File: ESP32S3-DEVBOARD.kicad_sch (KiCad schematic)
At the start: 61 parts, among them J1 PinHeader_1x22_P2.54mm_Vertic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, J2 PinHeader_1x22_P2.54mm_Vertic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, J3 G-Switch_GT-USB-7010ASV, J4 G-Switch_GT-USB-7010ASV, Q1 BC817-40,215, Q2 BC817-40,215, SW1 TS-1088-AR02016, SW2 TS-1088-AR02016, SW3 TS-1088-AR02016, SW4 TS-1088-AR02016, U1 AMS1117-3.3, U2 ESP32-S3-WROOM-1, U3 USBLC6-2P6, U4 CP2102N-A02-GQFN28R, U5 BMI270, U6 USBLC6-2P6

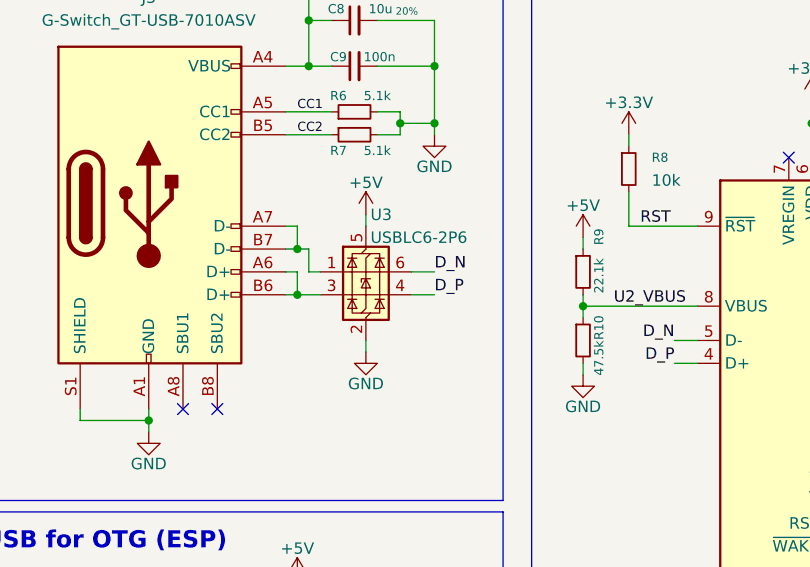
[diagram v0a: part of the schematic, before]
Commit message: Started to rout USB, need swap ports for uart
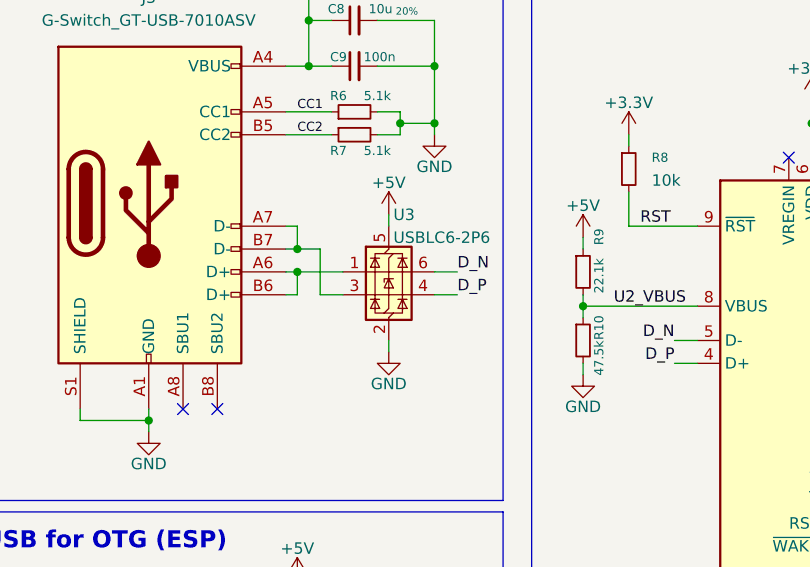
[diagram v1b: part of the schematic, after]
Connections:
- net at J3.A7 (D-), J3.B7 (D-): now also U3.3 (I/O2); no longer U3.1 (I/O1)
- net at J3.A6 (D+), J3.B6 (D+): now also U3.1 (I/O1); no longer U3.3 (I/O2)
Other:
- moved on the sheet: U3
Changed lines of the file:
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@@
 	)
 	(junction
+		(at 54.61 99.06)
+		(diameter 0)
+		(color 0 0 0 0)
+	)
+	(junction
 		(at 266.7 80.01)
 		(diameter 0)
@@
 	)
 	(junction
-		(at 54.61 101.6)
-		(diameter 0)
-		(color 0 0 0 0)
-	)
-	(junction
 		(at 185.42 123.19)
 		(diameter 0)
@@
 	(wire
 		(pts
-			(xy 64.77 147.32) (xy 64.77 148.59)
+			(xy 57.15 96.52) (xy 57.15 101.6)
 		)
 		(stroke
@@
 	(wire
 		(pts
-			(xy 208.28 39.37) (xy 209.55 39.37)
+			(xy 64.77 147.32) (xy 64.77 148.59)
 		)
 		(stroke
@@
 	(wire
 		(pts
-			(xy 54.61 101.6) (xy 57.15 101.6)
+			(xy 208.28 39.37) (xy 209.55 39.37)
 		)
 		(stroke
@@
 	(wire
 		(pts
-			(xy 67.31 99.06) (xy 69.85 99.06)
+			(xy 69.85 99.06) (xy 72.39 99.06)
 		)
 		(stroke
@@
 	(wire
 		(pts
-			(xy 62.23 106.68) (xy 62.23 107.95)
+			(xy 64.77 106.68) (xy 64.77 107.95)
 		)
 		(stroke
@@
 	(wire
 		(pts
-			(xy 55.88 99.06) (xy 57.15 99.06)
-		)
-		(stroke
-			(width 0)
-			(type default)
-		)
-	)
-	(wire
-		(pts
 			(xy 177.8 72.39) (xy 176.53 72.39)
 		)
@@
 	(wire
 		(pts
-			(xy 67.31 101.6) (xy 69.85 101.6)
+			(xy 69.85 101.6) (xy 72.39 101.6)
 		)
 		(stroke
@@
 	(wire
 		(pts
+			(xy 57.15 101.6) (xy 59.69 101.6)
+		)
+		(stroke
+			(width 0)
+			(type default)
+		)
+	)
+	(wire
+		(pts
 			(xy 177.8 62.23) (xy 176.53 62.23)
 		)
@@
 	(wire
 		(pts
-			(xy 62.23 92.71) (xy 62.23 93.98)
+			(xy 64.77 92.71) (xy 64.77 93.98)
 		)
 		(stroke
@@
 	(wire
 		(pts
-			(xy 55.88 96.52) (xy 55.88 99.06)
-		)
-		(stroke
-			(width 0)
-			(type default)
-		)
-	)
-	(wire
-		(pts
 			(xy 53.34 76.2) (xy 55.88 76.2)
 		)
@@
 	(wire
 		(pts
-			(xy 54.61 96.52) (xy 55.88 96.52)
+			(xy 54.61 96.52) (xy 57.15 96.52)
 		)
 		(stroke
@@
 	(wire
 		(pts
+			(xy 54.61 99.06) (xy 59.69 99.06)
+		)
+		(stroke
+			(width 0)
+			(type default)
+		)
+	)
+	(wire
+		(pts
 			(xy 54.61 163.83) (xy 55.88 163.83)
 		)
@@
 	)
 	(label "D_N"
-		(at 69.85 99.06 0)
+		(at 72.39 99.06 0)
 		(effects
 			(font
@@
 	)
 	(label "D_P"
-		(at 69.85 101.6 0)
+		(at 72.39 101.6 0)
 		(effects
 			(font
@@
 	(symbol
 		(lib_id "ESP32S3-DEVBOARD:USBLC6-2P6")
-		(at 62.23 99.06 0)
+		(at 64.77 99.06 0)
 		(unit 1)
 		(exclude_from_sim no)
@@
 		(dnp no)
 		(property "Reference" "U3"
-			(at 62.738 92.71 0)
+			(at 65.278 92.71 0)
 			(effects
 				(font
@@
 		)
 		(property "Value" "USBLC6-2P6"
-			(at 62.738 95.25 0)
+			(at 65.278 95.25 0)
 			(effects
 				(font
@@
 		)
 		(property "Footprint" "ESP32S3-DEVBOARD:SOT-666"
-			(at 63.246 105.791 0)
+			(at 65.786 105.791 0)
 			(effects
 				(font
@@
 		)
 		(property "Datasheet" "https://www.st.com/resource/en/datasheet/usblc6-2.pdf"
-			(at 63.246 107.696 0)
+			(at 65.786 107.696 0)
 			(effects
 				(font
@@
 		)
 		(property "Description" "Very low capacitance ESD protection diode, 2 data-line, SOT-666"
-			(at 62.23 99.06 0)
+			(at 64.77 99.06 0)
 			(effects
 				(font
@@
 		)
 		(property "Mfr. Part # " "USBLC6-2P6"
-			(at 62.23 99.06 0)
+			(at 64.77 99.06 0)
 			(effects
 				(font
@@
 		)
 		(property "LCSC" "C2827693"
-			(at 62.23 99.06 0)
+			(at 64.77 99.06 0)
 			(effects
 				(font
@@
 	(symbol
 		(lib_id "power:+5V")
-		(at 62.23 92.71 0)
+		(at 64.77 92.71 0)
 		(unit 1)
 		(exclude_from_sim no)
@@
 		(dnp no)
 		(property "Reference" "#PWR027"
-			(at 62.23 96.52 0)
+			(at 64.77 96.52 0)
 			(effects
 				(font
@@
 		)
 		(property "Value" "+5V"
-			(at 62.23 89.154 0)
+			(at 64.77 89.154 0)
 			(effects
 				(font
@@
 		)
 		(property "Footprint" ""
-			(at 62.23 92.71 0)
+			(at 64.77 92.71 0)
 			(effects
 				(font
@@
 		)
 		(property "Datasheet" ""
-			(at 62.23 92.71 0)
+			(at 64.77 92.71 0)
 			(effects
 				(font
@@
 		)
 		(property "Description" "Power symbol creates a global label with name \"+5V\""
-			(at 62.23 92.71 0)
+			(at 64.77 92.71 0)
 			(effects
 				(font
@@
 	(symbol
 		(lib_id "power:GND")
-		(at 62.23 107.95 0)
+		(at 64.77 107.95 0)
 		(unit 1)
 		(exclude_from_sim no)
@@
 		(dnp no)
 		(property "Reference" "#PWR030"
-			(at 62.23 114.3 0)
+			(at 64.77 114.3 0)
 			(effects
 				(font
@@
 		)
 		(property "Value" "GND"
-			(at 62.23 111.506 0)
+			(at 64.77 111.506 0)
 			(effects
 				(font
@@
 		)
 		(property "Footprint" ""
-			(at 62.23 107.95 0)
+			(at 64.77 107.95 0)
 			(effects
 				(font
@@
 		)
 		(property "Datasheet" ""
-			(at 62.23 107.95 0)
+			(at 64.77 107.95 0)
 			(effects
 				(font
@@
 		)
 		(property "Description" "Power symbol creates a global label with name \"GND\" , ground"
-			(at 62.23 107.95 0)
+			(at 64.77 107.95 0)
 			(effects
 				(font

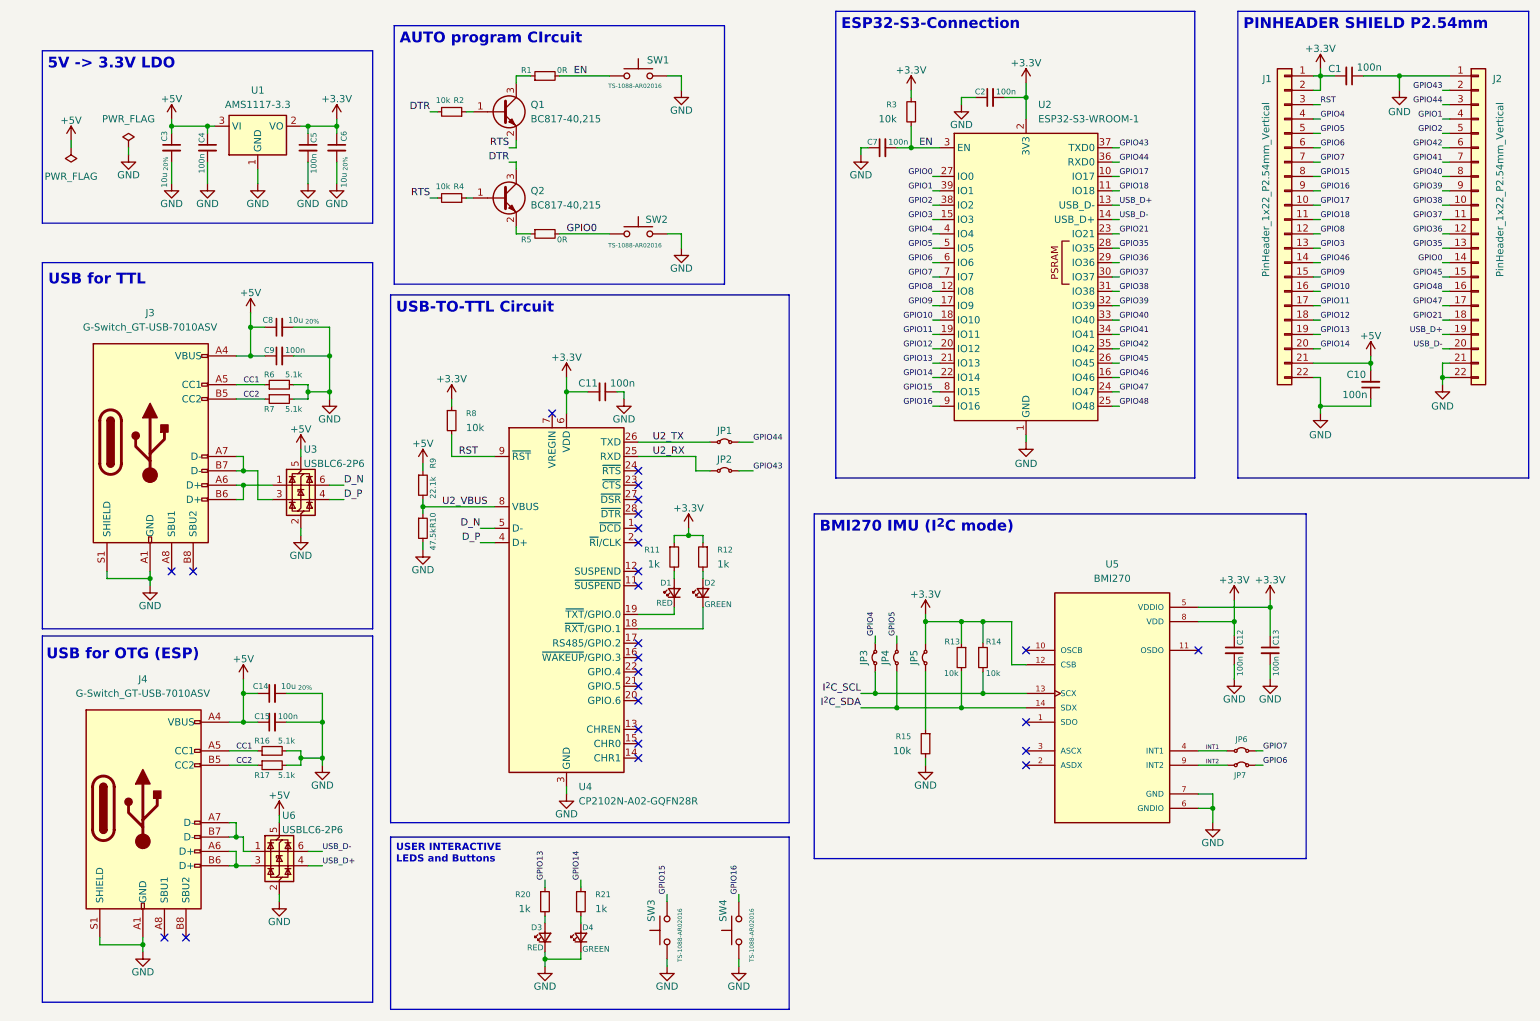
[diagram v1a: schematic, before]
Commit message: Defined netclasses for USB
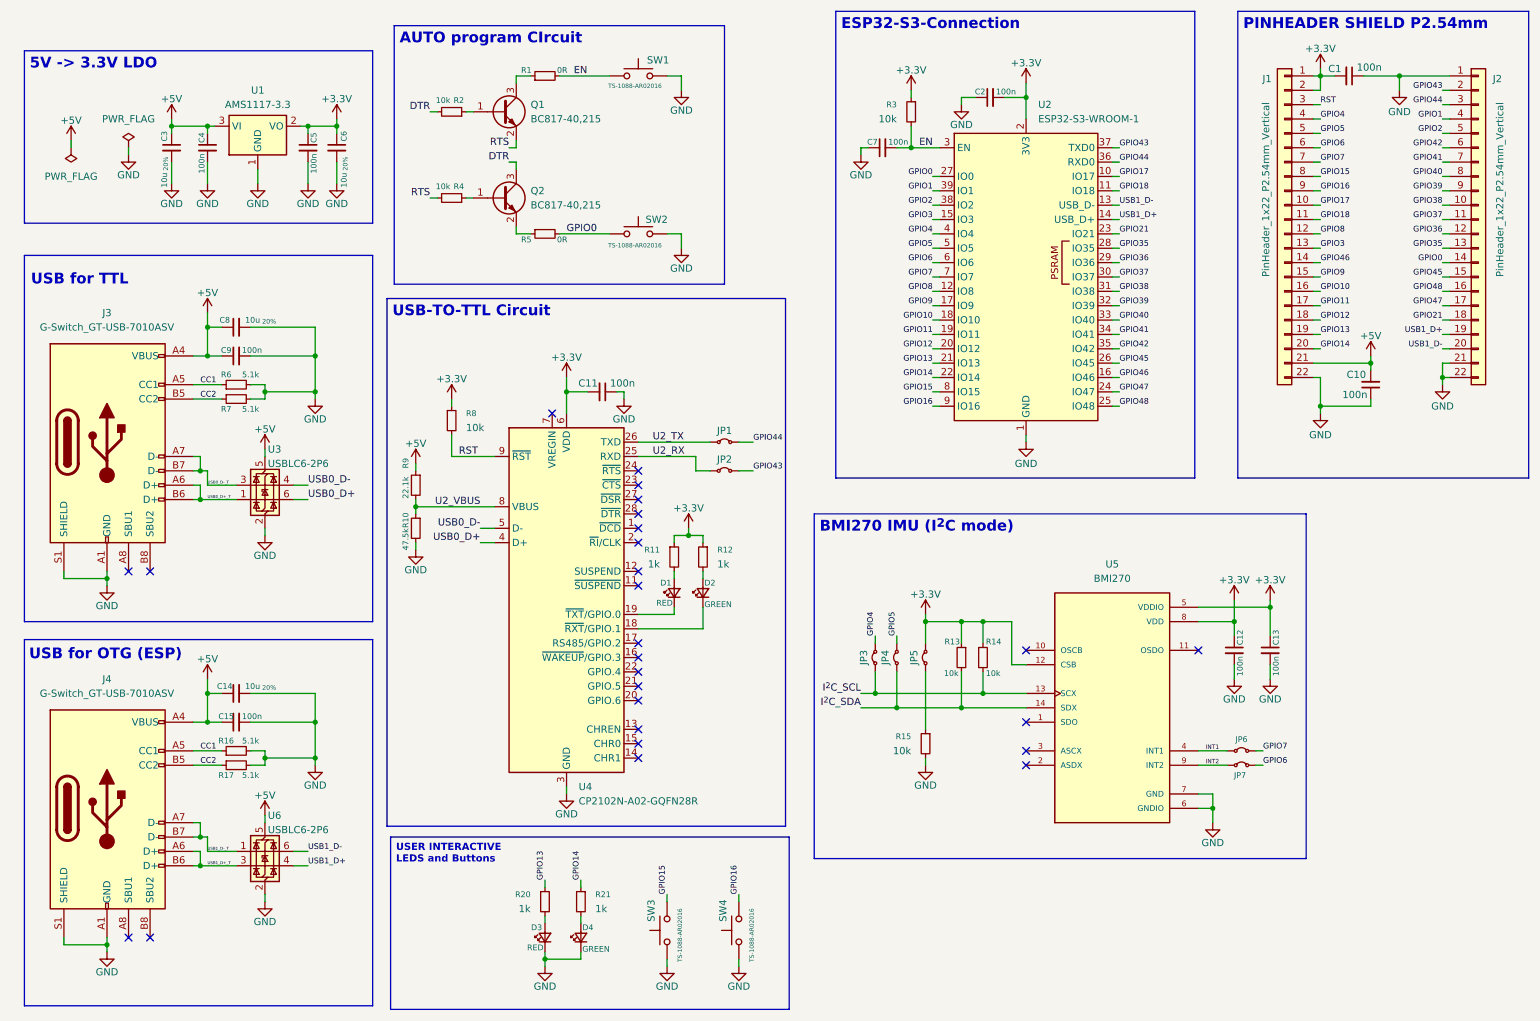
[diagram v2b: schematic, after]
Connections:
- net USB1_D+_T: now reaches J4.A6 (D+), J4.B6 (D+), U6.3 (I/O2)
- net USB1_D-_T: now reaches J4.A7 (D-), J4.B7 (D-), U6.1 (I/O1)
- net USB0_D+_T: now reaches J3.A6 (D+), J3.B6 (D+), U3.1 (I/O1)
- net USB0_D-_T: now reaches J3.A7 (D-), J3.B7 (D-), U3.3 (I/O2)
- net D_N renamed USB0_D+
- net USB0_D+: now also U4.4 (D+); no longer U4.5 (D-)
- net D_P renamed USB0_D-
- net USB0_D-: now also U4.5 (D-); no longer U4.4 (D+)
- net USB_D+ renamed USB1_D+
- net USB1_D+: now also U2.14 (USB_D+); no longer U2.13 (USB_D-)
- net USB_D- renamed USB1_D-
- net USB1_D-: now also U2.13 (USB_D-); no longer U2.14 (USB_D+)
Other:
- moved on the sheet: C14, C15, C8, C9, J3, J4, R10, R16, R17, R6, R7, R9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

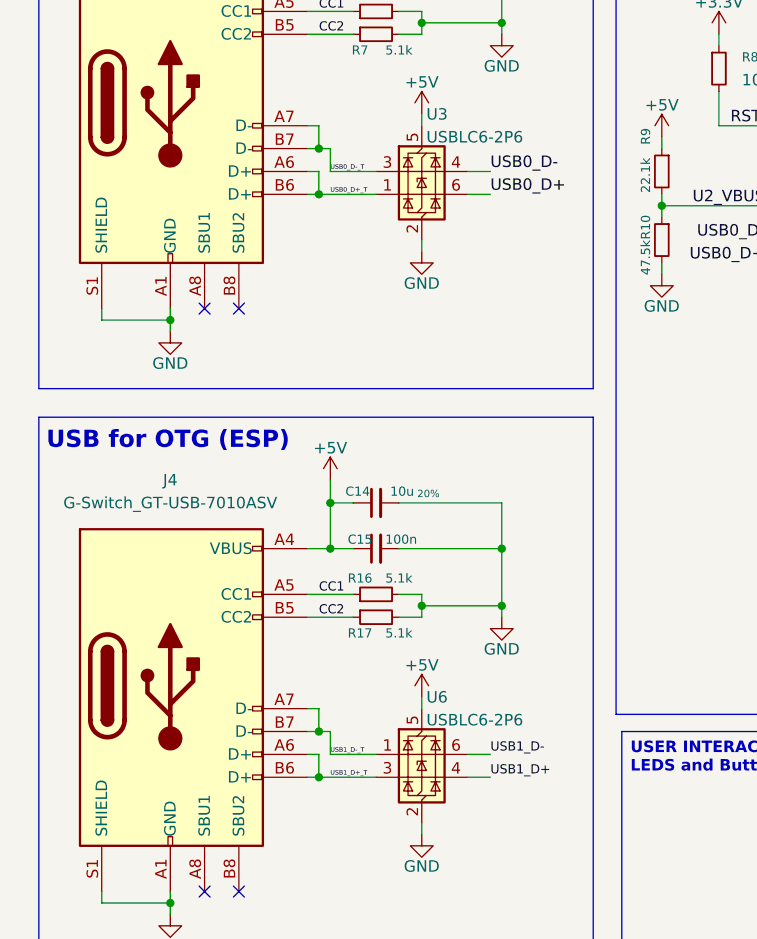
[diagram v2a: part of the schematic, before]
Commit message: Routed USB and added uart jumpers
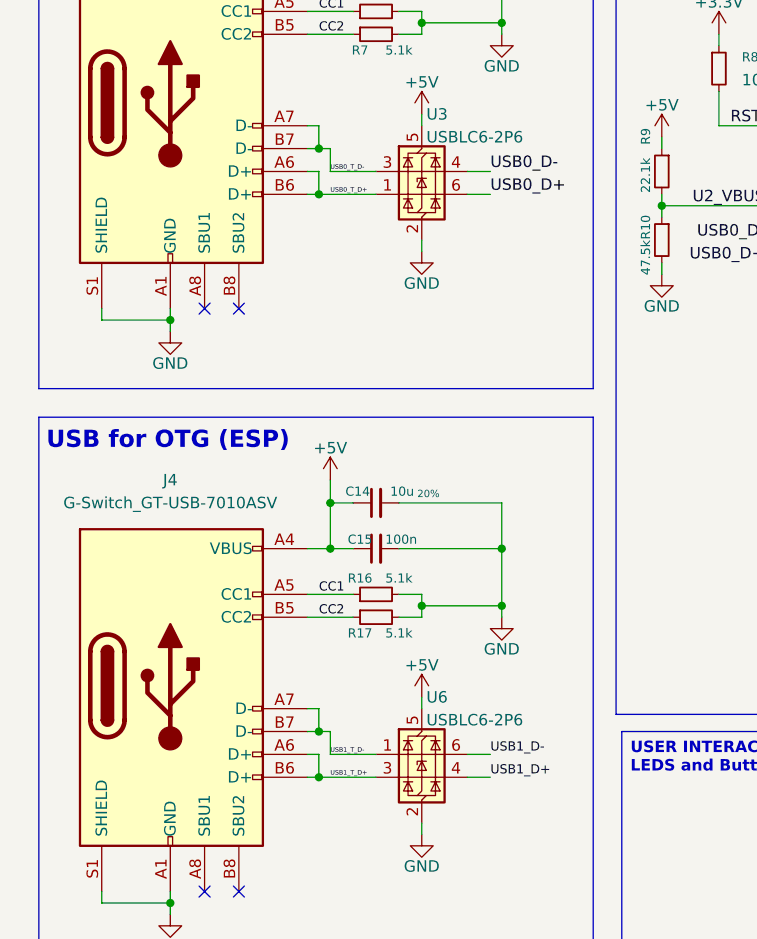
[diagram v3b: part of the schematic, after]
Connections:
- net USB0_D+_T renamed USB0_T_D+
- net USB0_D-_T renamed USB0_T_D-
- net USB1_D+_T renamed USB1_T_D+
- net USB1_D-_T renamed USB1_T_D-
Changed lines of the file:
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@@
 		)
 	)
-	(label "USB1_D-_T"
+	(label "USB1_T_D-"
 		(at 48.26 163.83 0)
 		(effects
@@
 		)
 	)
-	(label "USB0_D-_T"
+	(label "USB0_T_D-"
 		(at 48.26 99.06 0)
 		(effects
@@
 		)
 	)
-	(label "USB1_D+_T"
+	(label "USB1_T_D+"
 		(at 48.26 166.37 0)
 		(effects
@@
 		)
 	)
-	(label "USB0_D+_T"
+	(label "USB0_T_D+"
 		(at 48.26 101.6 0)
 		(effects
